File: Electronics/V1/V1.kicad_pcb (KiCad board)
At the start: 2 copper layers, 40 x 40 mm, 39 parts, among them J1 BATTERY, J3 GPIO, U2 TCA9517ADGK, U3 XIAO-ESP32-C3, U4 TPS72218, U5 ADPD1080, U7 TXB0102DCU, U8 MAX603

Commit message: Minor fixes
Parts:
- D4: value 3V3 LED -> CTRL LED
- LED1, PD1, PD2, PD3, PD4, U5: moved to B.Cu
- moved U3 113.8 mm to (34.5, 59.1)
- moved C11 103.2 mm to (56.7, 80.2)
- moved C12 103.2 mm to (56.7, 84.4)
- moved R10 103.2 mm to (37.7, 93.0)
- moved R6 103.2 mm to (37.7, 82.9)
- moved R7 103.2 mm to (37.7, 85.4)
- moved R8 103.2 mm to (37.7, 87.9)
- moved R9 103.2 mm to (37.7, 90.5)
- moved J1 103.2 mm to (28.1, 75.8)
- moved U2 103.2 mm to (26.2, 96.6)
- moved C1 103.2 mm to (24.7, 82.9)
- moved C10 103.2 mm to (29.0, 93.0)
- moved C2 103.2 mm to (24.7, 85.4)
- moved C3 103.2 mm to (24.7, 87.9)
- moved C4 103.2 mm to (24.7, 90.5)
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
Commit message: Some unfinished PCB changes
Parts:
- removed D2: B130LAW-7-F, Diode_SMD:D_SOD-123
- removed U8: MAX603, Package_DIP:DIP-8_W10.16mm_LongPads
- added H1: MountingHole, MountingHole:MountingHole_3.2mm_M3, F.Cu at (155.2, 79.5)
- added H2: MountingHole, MountingHole:MountingHole_3.2mm_M3, F.Cu at (205.2, 79.5)
- added Q1: PMV41XPAR, Package_TO_SOT_SMD:SOT-23, B.Cu at (183.8, 82.2)
- added Q3: PMV41XPAR, Package_TO_SOT_SMD:SOT-23, B.Cu at (154.8, 101.7)
- added R11: 10k, Resistor_SMD:R_0603_1608Metric_Pad0.98x0.95mm_HandSolder, B.Cu at (154.7, 97.8)
- added R12: 0R, Resistor_SMD:R_0603_1608Metric_Pad0.98x0.95mm_HandSolder, B.Cu at (158.0, 103.9)
- added SW1: PVA1 EE H1 3.5N V2, Button_Switch_THT:SW_Push_2P1T_Toggle_CK_PVA1xxH1xxxxxxV2, F.Cu at (153.8, 88.7)
- added U1: TPS7A4533, Package_TO_SOT_SMD:SOT-223-6, B.Cu at (166.3, 103.7)
- C1, C10, C2, C3, C4, C5, C6, C7, C8, C9, D1, D3, D4, R1, R10, R2, R3, R4, R5, R6, R9, U2, U4, U7: moved to B.Cu
- C11, C12: footprint Capacitor_SMD:C_1210_3225Metric_Pad1.33x2.70mm_HandSolder -> Capacitor_SMD:C_0805_2012Metric_Pad1.18x1.45mm_HandSolder; moved to B.Cu
- J1: value BATTERY -> BA9VPC; footprint TerminalBlock:TerminalBlock_bornier-2_P5.08mm -> Battery:BatteryHolder_MPD_BA9VPC_1xPP3
- R7: value 15k -> 20k; moved to B.Cu
- R8: value 12k -> 10k; moved to B.Cu
- moved C10 178.4 mm to (207.1, 104.4)
- moved C9 176.1 mm to (203.9, 111.6), turned to 180 degrees
- moved C5 173.2 mm to (197.0, 110.3)
- moved C3 172.3 mm to (196.3, 102.3)
- moved R5 170.6 mm to (203.6, 104.4), turned to 180 degrees
- moved C4 169.9 mm to (194.5, 95.9)
- moved C6 169.7 mm to (197.0, 107.1)
- moved C8 169.3 mm to (197.1, 108.7)
- moved R6 167.0 mm to (203.6, 102.5)
- moved U2 166.5 mm to (192.6, 100.1), turned to 90 degrees
- moved R1 162.6 mm to (194.5, 104.3), turned to 180 degrees
- moved D3 159.2 mm to (190.6, 78.1), turned to -90 degrees
- moved R2 158.8 mm to (191.0, 104.3)
- moved C7 158.0 mm to (185.4, 108.2)
- moved C2 153.2 mm to (177.2, 99.8), turned to 90 degrees
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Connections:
- C1 pad 1: +5V -> +3V3
- C12 pad 1: +5V -> +3V3
- C7 pad 1: VLED -> +3V3
- D1 pad 1: Net-(D1-K) -> VBAT
- D1 pad 2: +5V -> Net-(D1-A)
- J1 pad 2: /BAT- -> GND
- J3 pad 1: +5V -> +3V3
- J3 pad 2: GND -> +3V3
- J3 pad 3: +3V3 -> GND
- LED1 pad 2: VLED -> +3V3
- LED1 pad 5: VLED -> +3V3
- R9 pad 1: +3V3 -> Net-(Q1-S)
- U3 pad 12: +3V3 -> Net-(Q1-S)
- U3 pad 14: Net-(D1-K) -> VUSB
- U4 pad 1: +5V -> +3V3
- U4 pad 3: +5V -> +3V3
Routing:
- added copper zone on B.Cu, net +1V8
- added copper zone on B.Cu, net +3V3
- added copper zone on B.Cu, net GND
- added copper zone on F.Cu, net GND
- added copper zone on B.Cu, net VBAT
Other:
- board size 40 x 40 mm -> 60 x 55 mm

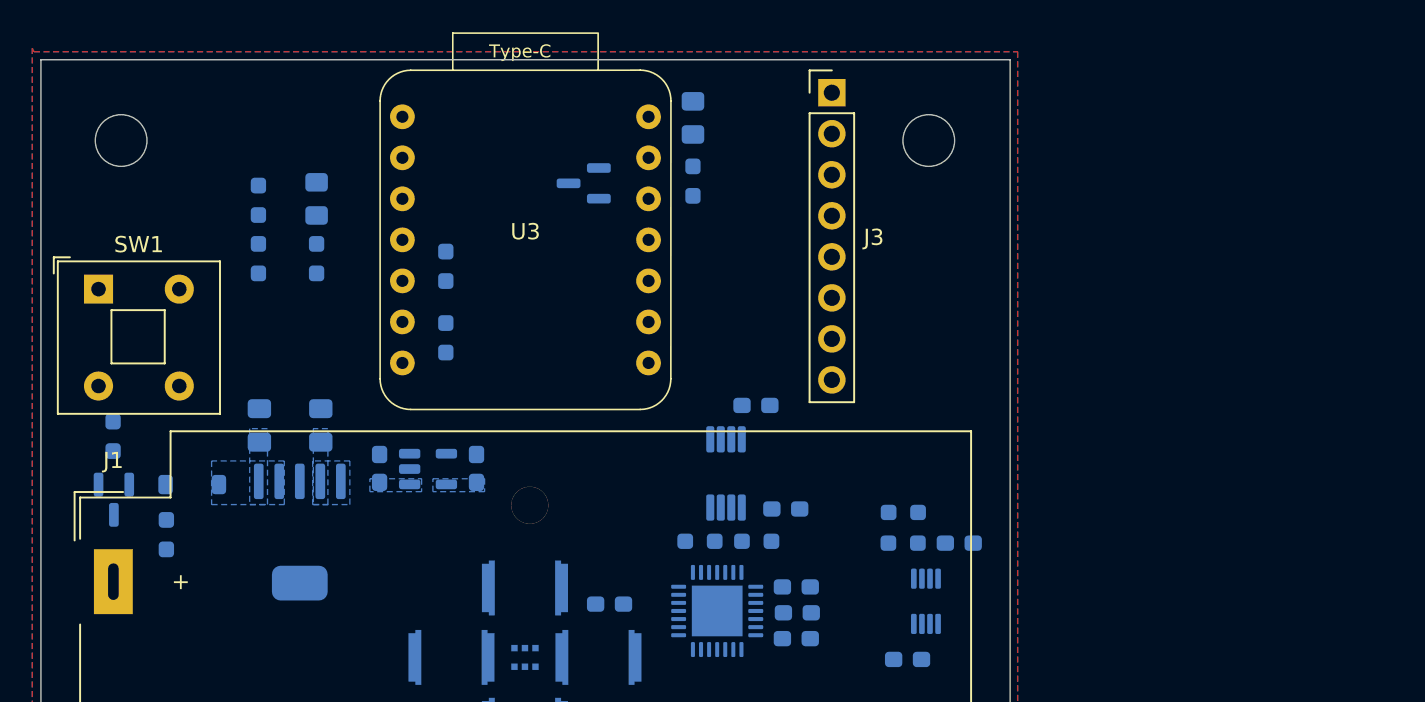
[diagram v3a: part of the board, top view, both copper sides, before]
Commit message: Swapped I2C shifter for PCA9306DC
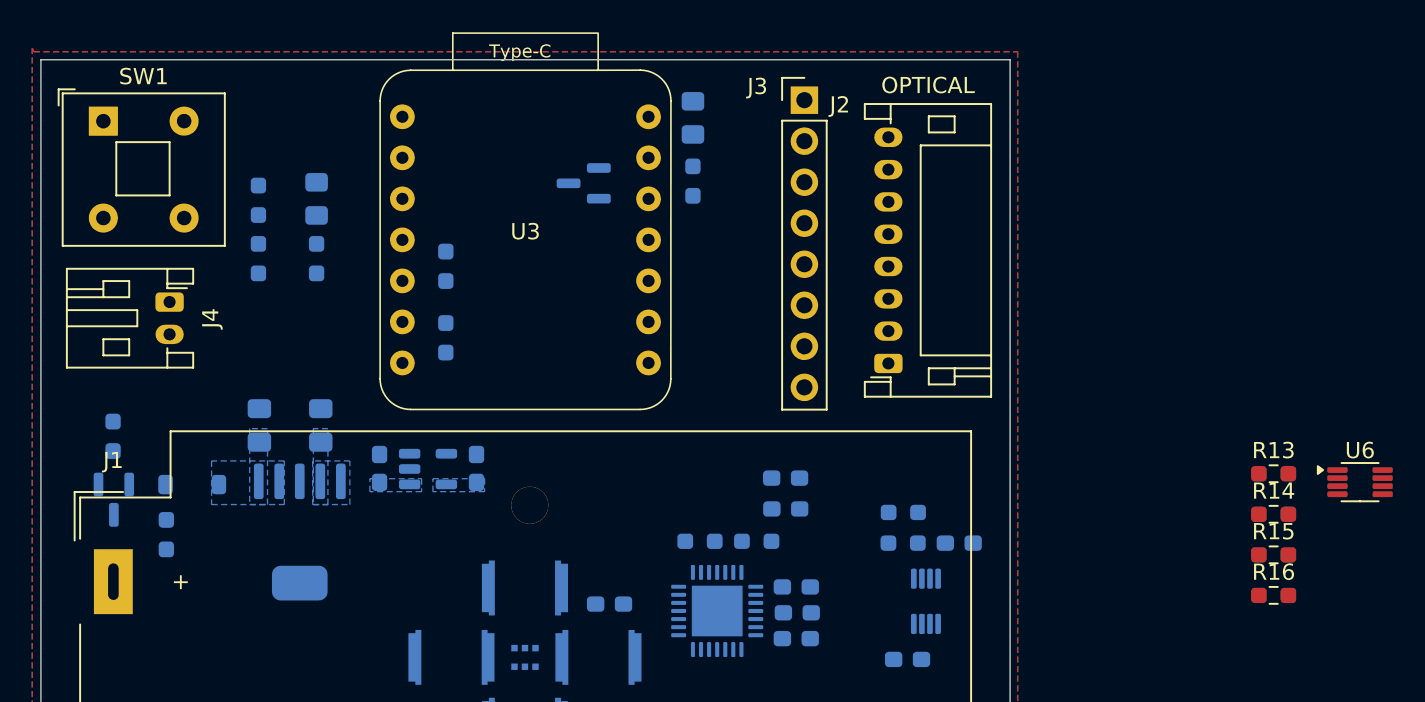
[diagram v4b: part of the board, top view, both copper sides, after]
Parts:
- removed H1, H2: MountingHole, MountingHole:MountingHole_3.2mm_M3
- removed U2: TCA9517ADGK, Package_SO:VSSOP-8_3x3mm_P0.65mm
- added J2: , Connector_JST:JST_PH_S8B-PH-K_1x08_P2.00mm_Horizontal, F.Cu at (202.7, 93.3)
- added J4: JST, Connector_JST:JST_PH_S2B-PH-K_1x02_P2.00mm_Horizontal, F.Cu at (158.2, 89.5)
- added R13: 10k, Resistor_SMD:R_0603_1608Metric_Pad0.98x0.95mm_HandSolder, F.Cu at (226.6, 100.1)
- added R14: 10k, Resistor_SMD:R_0603_1608Metric_Pad0.98x0.95mm_HandSolder, F.Cu at (226.6, 102.6)
- added R15: 200K, Resistor_SMD:R_0603_1608Metric_Pad0.98x0.95mm_HandSolder, F.Cu at (226.6, 105.2)
- added R16: 0, Resistor_SMD:R_0603_1608Metric_Pad0.98x0.95mm_HandSolder, F.Cu at (226.6, 107.7)
- added U6: PCA9306DC, Package_SO:VSSOP-8_2.3x2mm_P0.5mm, F.Cu at (231.9, 100.7)
- R5: value changeme -> 200k
- moved SW1 10.4 mm to (154.1, 78.3)
- moved C4 4.86 mm to (196.3, 100.4)
- moved J3 1.76 mm to (197.5, 77.0)
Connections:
- net Net-(LED1A-KIR) renamed /LED1
- net Net-(LED1B-KGREEN) renamed /LED2
- net Net-(LED1C-KRED) renamed /LED3
- net Net-(PD1-A) renamed /PD1
- net Net-(PD2-A) renamed /PD2
- net Net-(PD3-A) renamed /PD3
- net Net-(PD4-A) renamed /PD4
- C4 pad 1: +3V3 -> Net-(U6-VREF2)
- U3 pad 4: /I2C_EN -> unconnected-(U3-D3-Pad4)

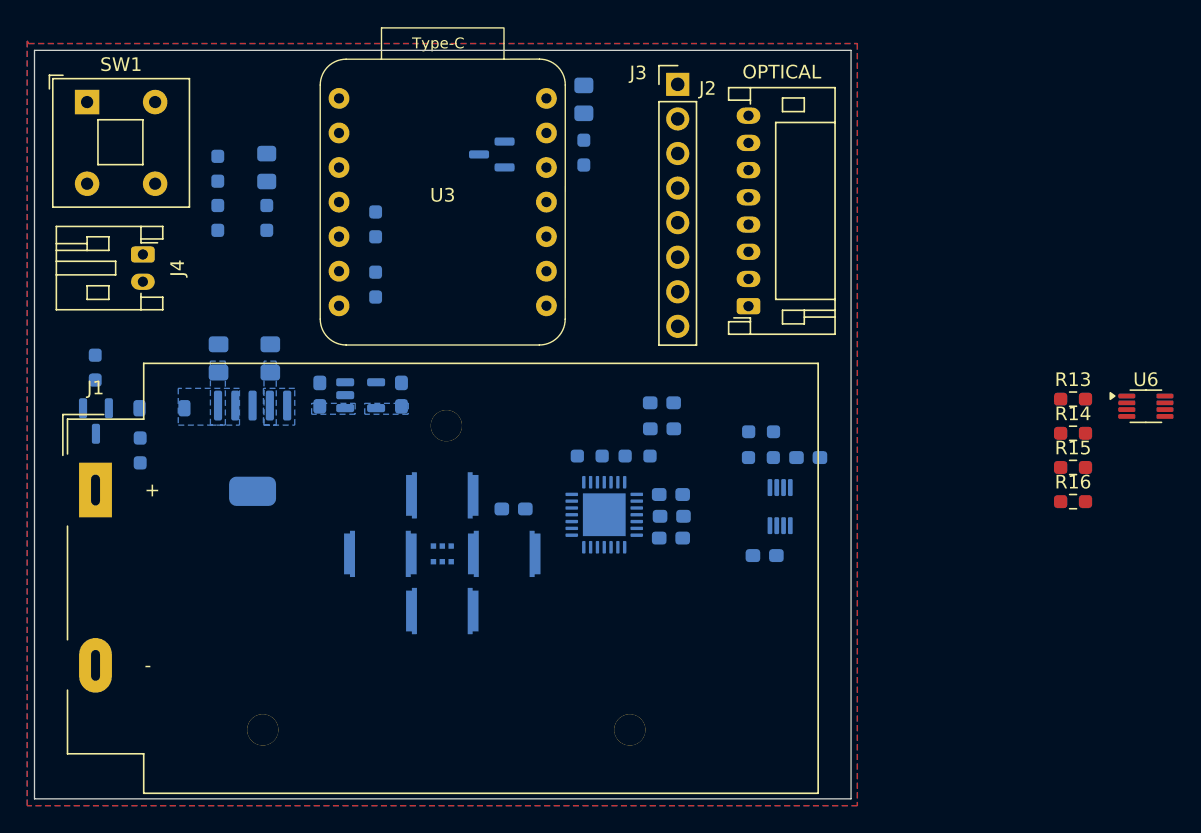
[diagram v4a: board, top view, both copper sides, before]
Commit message: Changing from integrated optical sensors to separate PCB
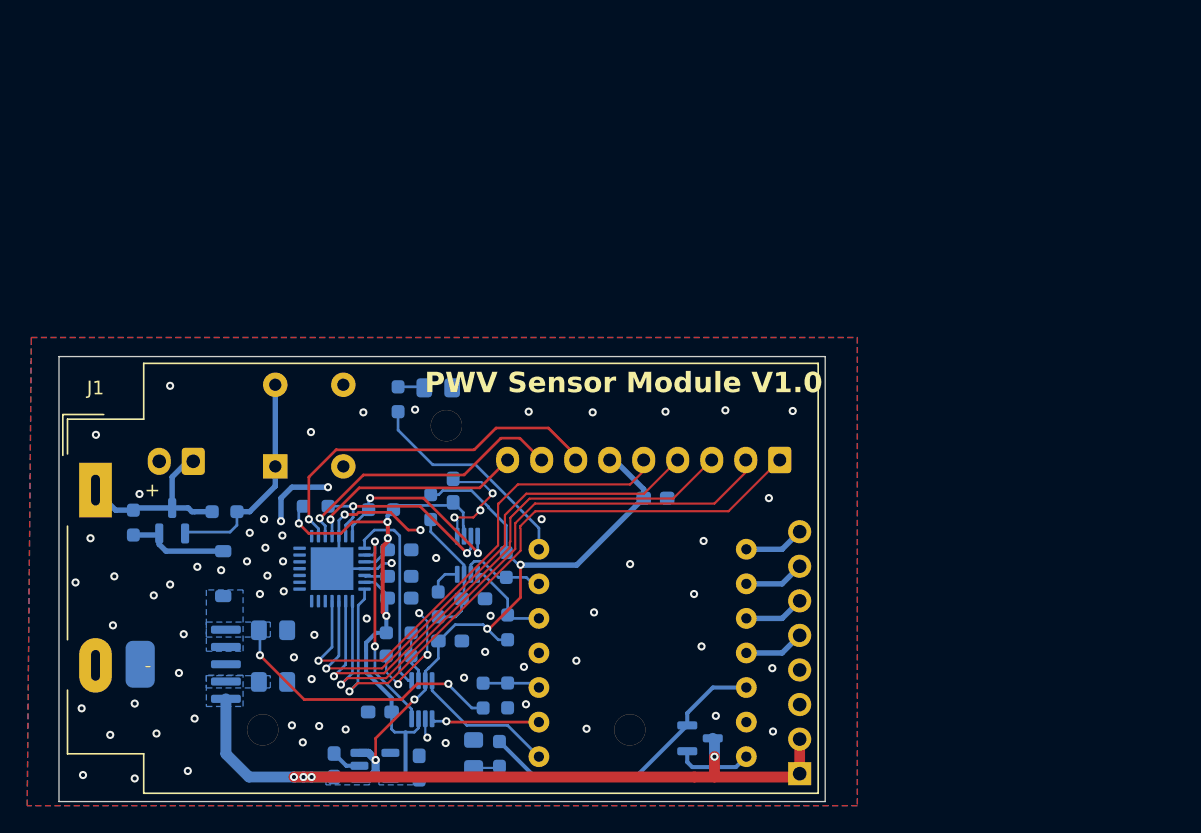
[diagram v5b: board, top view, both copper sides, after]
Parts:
- removed LED1: SFH-7016, CUSTOM:SFH-7016 Multi Chip LED
- removed PD1, PD2, PD3, PD4: SFH2200, CUSTOM:TOPLED D5140
- removed R13, R14: 10k, Resistor_SMD:R_0603_1608Metric_Pad0.98x0.95mm_HandSolder
- J2: value (none) -> OPTICAL; footprint Connector_JST:JST_PH_S8B-PH-K_1x08_P2.00mm_Horizontal -> Connector_JST:JST_EH_S9B-EH_1x09_P2.50mm_Horizontal; moved to B.Cu
- J3, R15, R16, SW1, U3, U6: moved to B.Cu
- J4: footprint Connector_JST:JST_PH_S2B-PH-K_1x02_P2.00mm_Horizontal -> Connector_JST:JST_EH_S2B-EH_1x02_P2.50mm_Horizontal; moved to B.Cu
- moved J3 51.4 mm to (206.5, 127.7)
- moved U6 51.0 mm to (182.1, 111.6), turned to -90 degrees
- moved D3 48.8 mm to (182.5, 126.2)
- moved R15 47.3 mm to (179.3, 108.1), turned to -90 degrees
- moved R16 47.3 mm to (179.9, 115.2), turned to 90 degrees
- moved Q1 45.5 mm to (199.1, 125.0), turned to 0 degrees
- moved R9 44.6 mm to (184.4, 126.2), turned to -90 degrees
- moved R8 44.2 mm to (185.0, 121.9), turned to -90 degrees
- moved R7 40.2 mm to (183.2, 121.9)
- moved U3 36.2 mm to (194.9, 118.8)
- moved R3 31.2 mm to (185.0, 116.9), turned to 90 degrees
- moved C9 30.5 mm to (175.6, 123.1)
- moved R6 30.4 mm to (177.0, 117.3)
- moved R5 30.4 mm to (177.0, 119.0)
- moved SW1 30.1 mm to (167.9, 105.1)
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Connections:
- J2 pad 5: +3V3 -> /PD_K
- J2 pad 6: /LED1 -> +3V3
- J2 pad 7: /LED2 -> /LED1
- J2 pad 8: /LED3 -> /LED2
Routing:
- net +3V3: track 0.00 -> 107.1 mm, vias 0 -> 8
- net /PD1: track 0.00 -> 47.7 mm, vias 0 -> 1
- net +1V8: track 0.00 -> 47.6 mm, vias 0 -> 4
- net /PD2: track 0.00 -> 44.7 mm, vias 0 -> 1
- net GND: track 0.00 -> 42.1 mm, vias 0 -> 77
- net /PD3: track 0.00 -> 41.5 mm, vias 0 -> 1
- net /PD4: track 0.00 -> 38.8 mm, vias 0 -> 1
- net /PD_K: track 0.00 -> 37.1 mm, vias 0 -> 1
- net /LED1: track 0.00 -> 26.9 mm, vias 0 -> 1
- net Net-(Q1-S): track 0.00 -> 22.6 mm
- net /LED2: track 0.00 -> 21.1 mm, vias 0 -> 1
- net VBAT: track 0.00 -> 20.9 mm, vias 0 -> 2
- net Net-(Q3-G): track 0.00 -> 16.3 mm
- net /UC_D6: track 0.00 -> 16.2 mm
- net /LED3: track 0.00 -> 16.2 mm, vias 0 -> 1
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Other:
- board size 60 x 55 mm -> 56.3 x 32.7 mm
- board text added: "PWV Sensor Module V1.0"

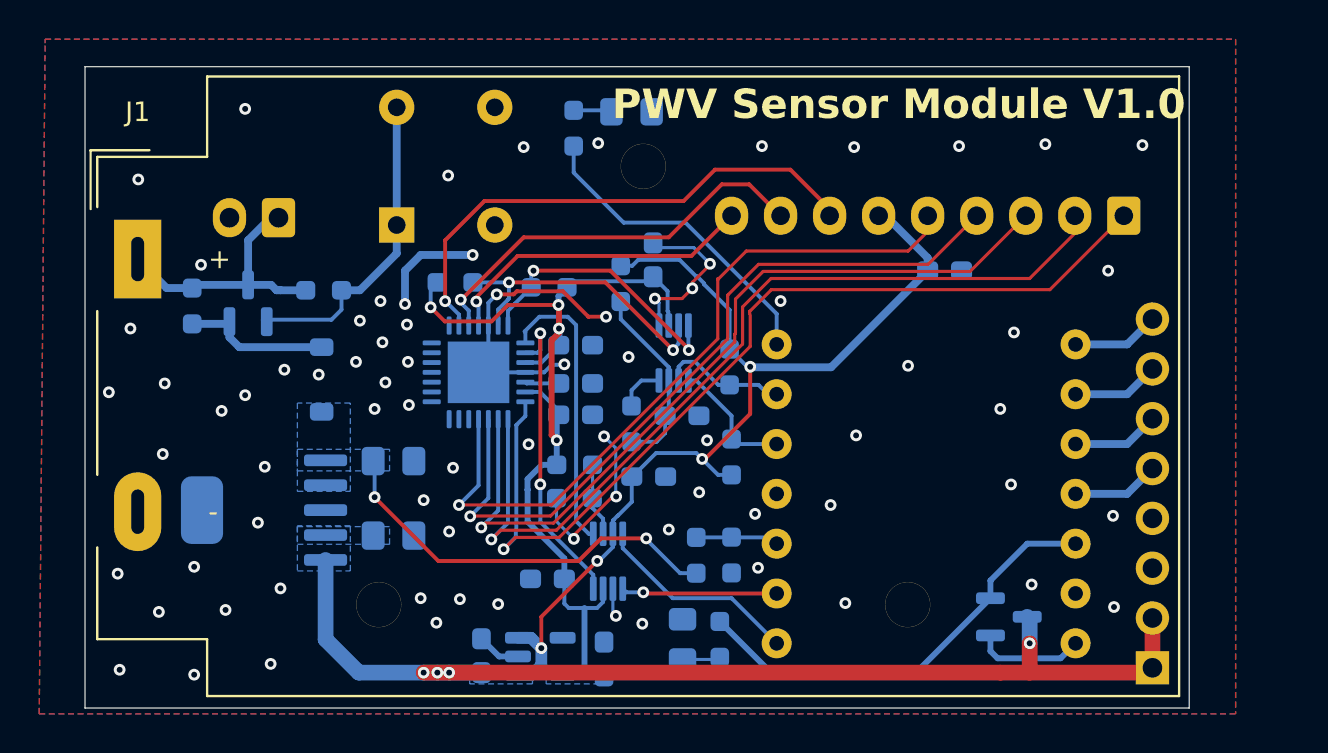
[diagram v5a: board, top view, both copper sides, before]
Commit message: Footprint changes
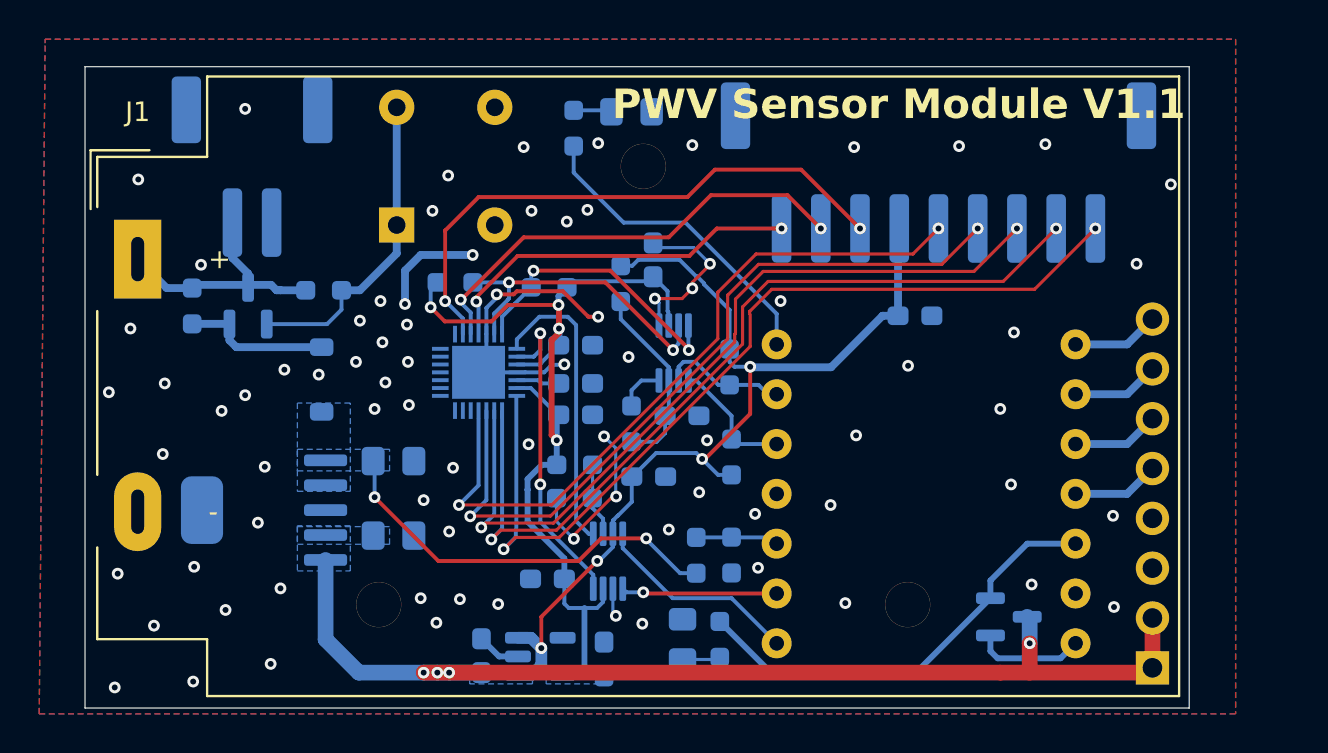
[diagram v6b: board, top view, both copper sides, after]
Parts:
- J2: footprint Connector_JST:JST_EH_S9B-EH_1x09_P2.50mm_Horizontal -> Connector_JST:JST_PH_S9B-PH-SM4-TB_1x09-1MP_P2.00mm_Horizontal
- J4: footprint Connector_JST:JST_EH_S2B-EH_1x02_P2.50mm_Horizontal -> Connector_JST:JST_PH_S2B-PH-SM4-TB_1x02-1MP_P2.00mm_Horizontal
- U5: footprint Package_CSP:LFCSP-28-1EP_5x5mm_P0.5mm_EP3.14x3.14mm -> CUSTOM:ADPD1080
- moved J2 9.70 mm to (195.6, 102.4), turned to 0 degrees
- moved J4 2.93 mm to (160.6, 102.1), turned to 0 degrees
- moved C7 2.75 mm to (194.3, 109.7)
- moved Q3 0.12 mm to (160.3, 109.2)
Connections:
- J2 pad 1: /PD1 -> /LED3
- J2 pad 2: /PD2 -> /LED2
- J2 pad 3: /PD3 -> /LED1
- J2 pad 4: /PD4 -> +3V3
- J2 pad 6: +3V3 -> /PD4
- J2 pad 7: /LED1 -> /PD3
- J2 pad 8: /LED2 -> /PD2
- J2 pad 9: /LED3 -> /PD1
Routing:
- net /LED1: track 26.9 -> 29.4 mm, vias 1 -> 2
- net /LED2: track 21.1 -> 23.4 mm, vias 1 -> 2
- net /LED3: track 16.2 -> 18.5 mm, vias 1 -> 2
- net +3V3: track 107.1 -> 105.4 mm
- net /PD1: track 47.7 -> 46.1 mm, vias 1 -> 2
- net /PD2: track 44.7 -> 43.3 mm, vias 1 -> 2
- net +1V8: track 47.6 -> 48.5 mm
- net /BAT+: track 13.7 -> 12.9 mm
- net /PD_K: track 37.1 -> 36.5 mm, vias 1 -> 2
- net /PPG_SDA: track 14.2 -> 14.8 mm
- net /AFE_1: track 15.9 -> 16.4 mm
- net /PPG_SCL: track 15.4 -> 15.9 mm
- net /PD3: track 41.5 -> 41.1 mm, vias 1 -> 2
- net GND: track 42.1 -> 42.4 mm, vias 77 -> 81
- net /PD4: track 38.8 -> 39.0 mm, vias 1 -> 2
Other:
- board text added: "PWV Sensor Module V1.1"
- board text added: "PWV V1.1"
- board text removed: "PWV Sensor Module V1.0"
